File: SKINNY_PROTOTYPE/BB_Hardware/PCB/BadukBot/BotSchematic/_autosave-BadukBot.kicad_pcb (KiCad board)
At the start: 4 copper layers, 22.4 x 96.8 mm, 74 parts, among them J1 MOLEX_78171-0002, J10 A3-16DA-2SV(71), J11 62401621722, J12 803-87-010-10-001101, J13 67997-410HLF, J2 MOLEX_78171-0003, Q1 MMBT3904LT1G, Q2 MMBT3904LT1G, Q3 MMBT3904LT1G, Q4 MMBT3904LT1G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

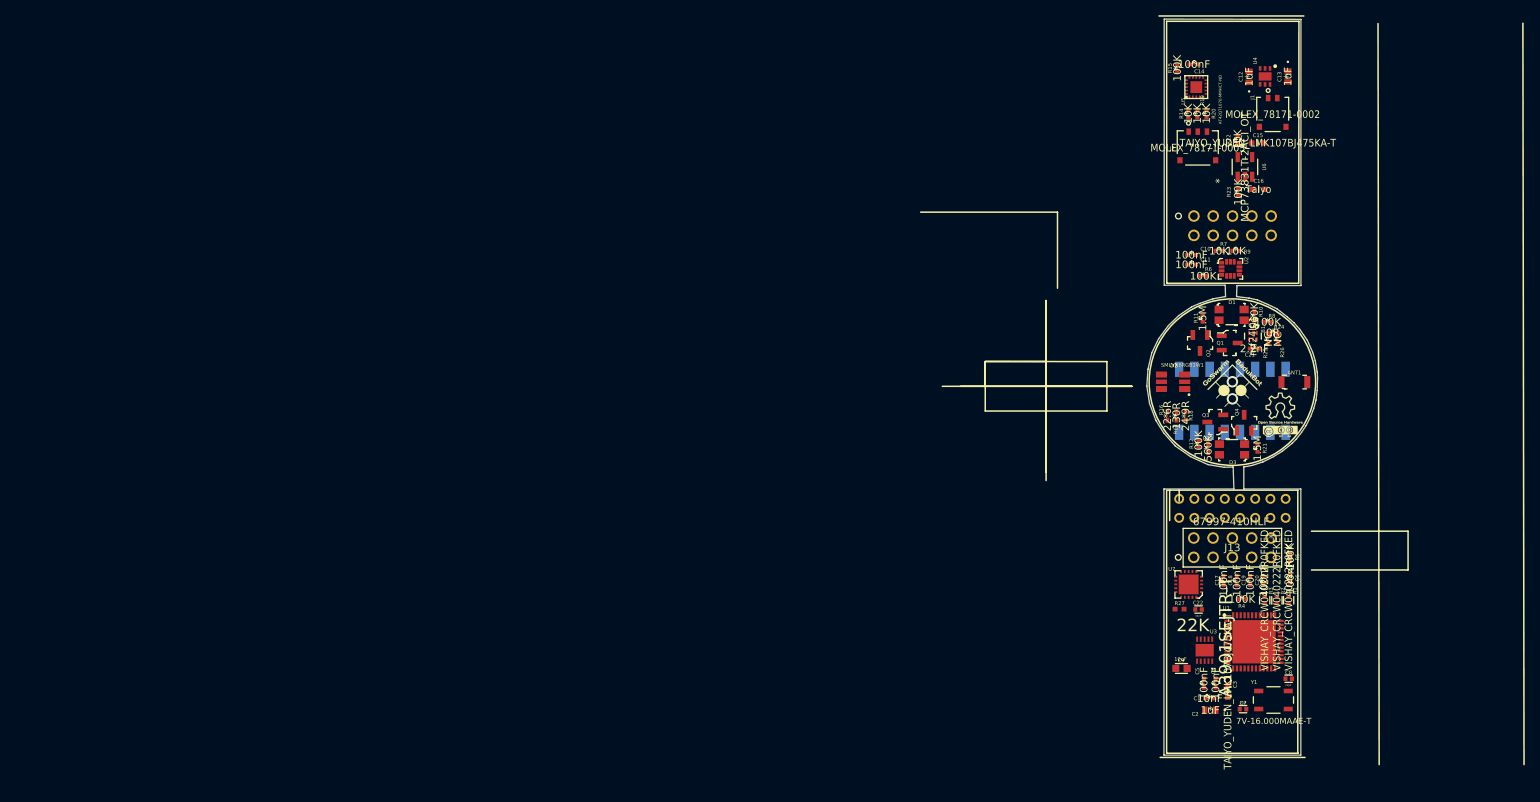
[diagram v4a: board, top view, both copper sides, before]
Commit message: Images of original board's layers; images of current work setup; updated schematics and BOM to change connectors; major boards revisions
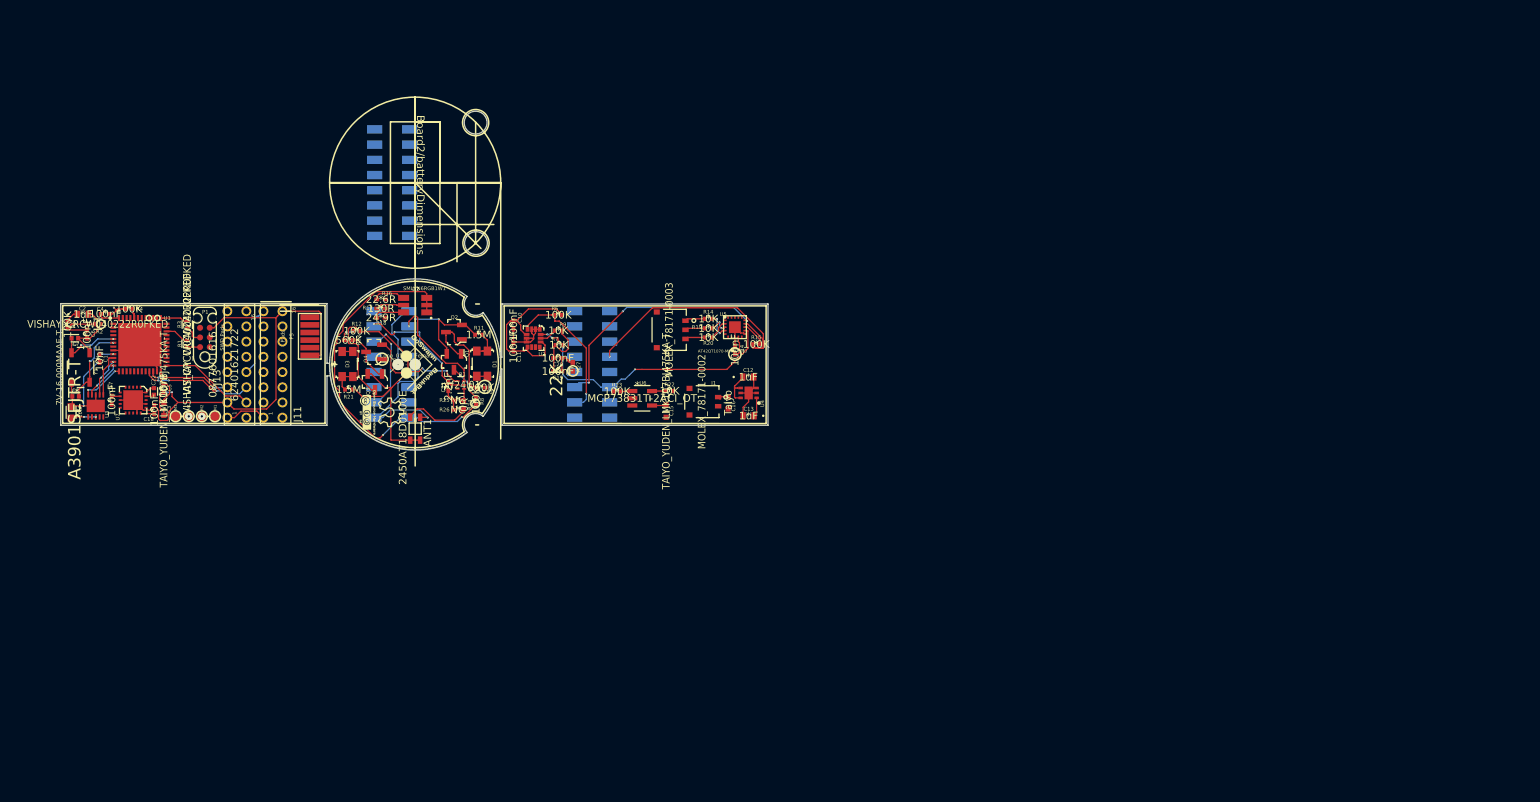
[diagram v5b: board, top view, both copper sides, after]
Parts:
- added J12: A3-16DA-2SV(71), A13:A13, B.Cu at (112.5, 86.3)
- added M1: Pos-1a, gsg-modules:TESTPOINT-50MIL, F.Cu at (88.6, 117.0)
- added M2: Neg-1a, gsg-modules:TESTPOINT-50MIL, F.Cu at (86.9, 117.0)
- added M3: Pos-2a, gsg-modules:TESTPOINT-50MIL, F.Cu at (83.4, 117.0)
- added M4: Neg-2a, gsg-modules:TESTPOINT-50MIL, F.Cu at (85.2, 117.0)
- added P1: SWD Pads, library:SWD_6pin, F.Cu at (87.3, 106.7)
- added P4: Conn_01x02_Female, Connector_DIN:Conn_01x02_Female, F.Cu at (113.8, 110.2)
- added P5: Pads, library:ExternalPort, F.Cu at (101.1, 106.5)
- ANT1: value Antenna -> 2450AT18D0100E; footprint digikey-footprints:Antenna_1.6x3.2mm_2450AT18A100E -> 2450AT18D0100E:DFN320X160X120-4RN
- J10: footprint 16pos_2mm_SMD:A13 -> A13:A13
- J11: moved to F.Cu
- J12: value 803-87-010-10-001101 -> A3-16DA-2SV(71); footprint 2x5conn:2x5 -> A13:A13
- J13: value 67997-410HLF -> 0877601616; footprint 2x5conn:2x5 -> 16pos_2mm_RA:0877601616
- U5: footprint AT42QT1070-MMHCT-ND:VQFN_20PAD -> vq:VQFN_20PAD
- moved C8 163.8 mm to (70.3, 114.4), turned to 180 degrees
- moved R5 163.6 mm to (69.2, 105.0)
- moved Y1 162.8 mm to (70.9, 110.6), turned to 270 degrees
- moved C6 161.4 mm to (71.8, 106.2)
- moved C7 161.2 mm to (70.2, 106.8), turned to 0 degrees
- moved R2 159.3 mm to (73.2, 104.9), turned to 180 degrees
- moved C2 157.1 mm to (71.2, 103.6), turned to 0 degrees
- moved C4 153.9 mm to (74.2, 103.6), turned to 0 degrees
- moved C1 152.7 mm to (73.4, 109.4), turned to 270 degrees
- moved U1 151.6 mm to (78.7, 107.6)
- moved R4 151.3 mm to (77.3, 102.9)
- moved C9 149.8 mm to (69.7, 116.5), turned to 90 degrees
- moved U3 149.3 mm to (72.9, 115.7), turned to 270 degrees
- moved R1 148.7 mm to (84.9, 107.5), turned to 90 degrees
- moved C17 148.1 mm to (75.0, 114.9)
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- renumbered G*** to G1, G*** to G2
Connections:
- net 10a_SDA renamed Net-(J10-Pad10)
- net 11a_SCL renamed Net-(J10-Pad11)
- net 15a_GND2 renamed Net-(J10-Pad16)
- net 8a_IO1 renamed Net-(J10-Pad8)
- net 9a_IO2 renamed Net-(J10-Pad9)
- ANT1 pad 2: Net-(ANT1-Pad2) -> 2a_GND
- C1 pad 2: 15b_GND2 -> 2b_GND
- C10 pad 2: 23a_GND -> 21a_3.3v
- C11 pad 2: 23a_GND -> 21a_3.3v
- C12 pad 2: 23a_GND -> 21a_3.3v
- C13 pad 2: 23a_GND -> 21a_3.3v
- C14 pad 2: 23a_GND -> 21a_3.3v
- C15 pad 2: 23a_GND -> 21a_3.3v
- C16 pad 2: 23a_GND -> 21a_3.3v
- C17 pad 1: 15b_GND2 -> 2b_GND
- C18 pad 1: 15b_GND2 -> 2b_GND
- C19 pad 1: 15b_GND2 -> 2b_GND
- C2 pad 2: 15b_GND2 -> 2b_GND
- C20 pad 1: 15b_GND2 -> 2b_GND
- C22 pad 2: 15b_GND2 -> 2b_GND
- C3 pad 2: 15b_GND2 -> 2b_GND
- C4 pad 2: 15b_GND2 -> 2b_GND
- C5 pad 2: 15b_GND2 -> 2b_GND
- C6 pad 2: 15b_GND2 -> 2b_GND
- C7 pad 2: 15b_GND2 -> 2b_GND
- C8 pad 2: 15b_GND2 -> 2b_GND
- C9 pad 2: 15b_GND2 -> 2b_GND
- J1 pad 2: 23a_GND -> 21a_3.3v
- J11 pad 10: 10b_SDA -> Net-(J11-Pad10)
- J11 pad 11: 11b_SCL -> Net-(J11-Pad11)
- J11 pad 16: 15b_GND2 -> 2b_GND
- J11 pad 2: 15b_GND2 -> Net-(J11-Pad2)
- J11 pad 8: 8b_IO1 -> Net-(J11-Pad8)
- J11 pad 9: 9b_IO2 -> Net-(J11-Pad9)
- J12 pad 10: 21a_3.3v -> Net-(J12-Pad10)
- J12 pad 2: 22a_VBAT -> 21a_3.3v
- J12 pad 3: 23a_GND -> 22a_VBAT
- J13 pad 10: 1b_3.3v -> Net-(J13-Pad10)
- J13 pad 3: 15b_GND2 -> 2b_GND
- R16 pad 1: 6a_RGBLED2 -> Net-(R16-Pad1)
- R17 pad 1: 5a_RGBLED1 -> Net-(R17-Pad1)
- R18 pad 1: 7a_RGBLED3 -> Net-(R18-Pad1)
- R22 pad 1: 23a_GND -> 21a_3.3v
- R27 pad 1: 15b_GND2 -> 2b_GND
- R4 pad 2: 15b_GND2 -> 2b_GND
- U1 pad 23: 15b_GND2 -> 2b_GND
- U1 pad 47: 15b_GND2 -> 2b_GND
- U1 pad 49: 15b_GND2 -> 2b_GND
- U1 pad 8: 15b_GND2 -> 2b_GND
- U2 pad 1: 23a_GND -> 21a_3.3v
- U2 pad 2: 23a_GND -> 21a_3.3v
- U2 pad 3: 23a_GND -> 21a_3.3v
- U2 pad 6: 23a_GND -> 21a_3.3v
- U2 pad 7: 23a_GND -> 21a_3.3v
- U2 pad 9: Net-(U2-Pad9) -> 21a_3.3v
- U3 pad 11: Net-(U3-Pad11) -> 2b_GND
- U3 pad 3: Net-(U3-Pad3) -> 2b_GND
- U4 pad 2: Net-(U4-Pad2) -> 21a_3.3v
- U4 pad 3: 23a_GND -> 21a_3.3v
- U4 pad 5: Net-(U4-Pad5) -> 21a_3.3v
- U4 pad 7: Net-(U4-Pad7) -> 21a_3.3v
- U5 pad 11: 23a_GND -> 21a_3.3v
- U5 pad 13: 23a_GND -> 21a_3.3v
- U5 pad 8: 23a_GND -> 21a_3.3v
- U5 pad 9: 23a_GND -> 21a_3.3v
- U6 pad 2: 23a_GND -> 21a_3.3v
- U7 pad 14: 15b_GND2 -> 2b_GND
- U7 pad 17: 15b_GND2 -> 2b_GND
- U7 pad 20: 15b_GND2 -> 2b_GND
- U7 pad 21: 15b_GND2 -> 2b_GND
- U7 pad 8: 15b_GND2 -> 2b_GND
- Y1 pad 2: Net-(Y1-Pad2) -> 2b_GND
- Y1 pad 4: Net-(Y1-Pad4) -> 2b_GND
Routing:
- net 2b_GND: track 0.00 -> 111.4 mm, vias 0 -> 5
- net 15a_GND2: track 0.00 -> 70.6 mm, vias 0 -> 4
- net 21a_3.3v: track 0.00 -> 53.6 mm
- net 1a_3.3v: track 0.00 -> 53.5 mm, vias 0 -> 4
- net 25a_SDA: track 0.00 -> 37.4 mm, vias 0 -> 4
- net ~29a_TOUCH_CHG~: track 0.00 -> 34.4 mm, vias 0 -> 1
- net 26a_SCL: track 0.00 -> 33.4 mm, vias 0 -> 3
- net 1b_3.3v: track 0.00 -> 31.8 mm, vias 0 -> 4
- net 4a_PHOTODIODE2: track 0.00 -> 25.8 mm, vias 0 -> 1
- net 24a_IMU_INT: track 0.00 -> 19.5 mm, vias 0 -> 1
- net 14a_VDD_PA: track 0.00 -> 16.4 mm, vias 0 -> 3
- net 12a_ANT1: track 0.00 -> 15.5 mm, vias 0 -> 3
- net 11b_SCL: track 0.00 -> 14.7 mm, vias 0 -> 3
- net Net-(Q1-Pad1): track 0.00 -> 14.1 mm
- net 13a_ANT2: track 0.00 -> 13.9 mm, vias 0 -> 1
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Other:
- board size 22.4 x 96.8 mm -> 93 x 44.5 mm
- board text added: "Board1/3HeaderDimensions"
- board text added: "Board1_topDownFootprint"
- board text added: "Board2/batteryDimensions"
- board text added: "Board3_topDownFootprint"
